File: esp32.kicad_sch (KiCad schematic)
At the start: 24 parts, among them J12 DAT0, J13 DAT_DSP, J14 + -, Q18 2N3904, Q19 2N3904, Q20 2N3904, U10 74LS241, U11 74LS241, U12 74LS241, U15 74LS241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

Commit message: smaller resistor footprint
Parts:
- R100, R90, R91, R95, R96, R97, R98, R99: footprint Resistor_THT:R_Axial_DIN0207_L6.3mm_D2.5mm_P10.16mm_Horizontal -> Resistor_THT:R_Axial_DIN0207_L6.3mm_D2.5mm_P2.54mm_Vertical
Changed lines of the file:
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@@
     (property "Reference" "R95" (id 0) (at 110.49 121.0142 90))
     (property "Value" "1k" (id 1) (at 110.49 123.5511 90))
-    (property "Footprint" "Resistor_THT:R_Axial_DIN0207_L6.3mm_D2.5mm_P10.16mm_Horizontal" (id 2) (at 110.49 127.508 90)
+    (property "Footprint" "Resistor_THT:R_Axial_DIN0207_L6.3mm_D2.5mm_P2.54mm_Vertical" (id 2) (at 110.49 127.508 90)
       (effects (font (size 1.27 1.27)) hide)
     )
@@
       (effects (font (size 1.27 1.27)) (justify left))
     )
-    (property "Footprint" "Resistor_THT:R_Axial_DIN0207_L6.3mm_D2.5mm_P10.16mm_Horizontal" (id 2) (at 122.682 114.3 90)
+    (property "Footprint" "Resistor_THT:R_Axial_DIN0207_L6.3mm_D2.5mm_P2.54mm_Vertical" (id 2) (at 122.682 114.3 90)
       (effects (font (size 1.27 1.27)) hide)
     )
@@
       (effects (font (size 1.27 1.27)) (justify left))
     )
-    (property "Footprint" "Resistor_THT:R_Axial_DIN0207_L6.3mm_D2.5mm_P10.16mm_Horizontal" (id 2) (at 99.822 63.5 90)
+    (property "Footprint" "Resistor_THT:R_Axial_DIN0207_L6.3mm_D2.5mm_P2.54mm_Vertical" (id 2) (at 99.822 63.5 90)
       (effects (font (size 1.27 1.27)) hide)
     )
@@
       (effects (font (size 1.27 1.27)) (justify left))
     )
-    (property "Footprint" "Resistor_THT:R_Axial_DIN0207_L6.3mm_D2.5mm_P10.16mm_Horizontal" (id 2) (at 134.112 168.91 90)
+    (property "Footprint" "Resistor_THT:R_Axial_DIN0207_L6.3mm_D2.5mm_P2.54mm_Vertical" (id 2) (at 134.112 168.91 90)
       (effects (font (size 1.27 1.27)) hide)
     )
@@
     (property "Reference" "R96" (id 0) (at 111.76 53.7042 90))
     (property "Value" "1k" (id 1) (at 111.76 56.2411 90))
-    (property "Footprint" "Resistor_THT:R_Axial_DIN0207_L6.3mm_D2.5mm_P10.16mm_Horizontal" (id 2) (at 111.76 60.198 90)
+    (property "Footprint" "Resistor_THT:R_Axial_DIN0207_L6.3mm_D2.5mm_P2.54mm_Vertical" (id 2) (at 111.76 60.198 90)
       (effects (font (size 1.27 1.27)) hide)
     )
@@
       (effects (font (size 1.27 1.27)) (justify left))
     )
-    (property "Footprint" "Resistor_THT:R_Axial_DIN0207_L6.3mm_D2.5mm_P10.16mm_Horizontal" (id 2) (at 98.552 130.81 90)
+    (property "Footprint" "Resistor_THT:R_Axial_DIN0207_L6.3mm_D2.5mm_P2.54mm_Vertical" (id 2) (at 98.552 130.81 90)
       (effects (font (size 1.27 1.27)) hide)
     )
@@
       (effects (font (size 1.27 1.27)) (justify left))
     )
-    (property "Footprint" "Resistor_THT:R_Axial_DIN0207_L6.3mm_D2.5mm_P10.16mm_Horizontal" (id 2) (at 123.952 46.99 90)
+    (property "Footprint" "Resistor_THT:R_Axial_DIN0207_L6.3mm_D2.5mm_P2.54mm_Vertical" (id 2) (at 123.952 46.99 90)
       (effects (font (size 1.27 1.27)) hide)
     )
@@
     (property "Reference" "R100" (id 0) (at 149.86 175.6242 90))
     (property "Value" "220k" (id 1) (at 149.86 178.1611 90))
-    (property "Footprint" "Resistor_THT:R_Axial_DIN0207_L6.3mm_D2.5mm_P10.16mm_Horizontal" (id 2) (at 149.86 182.118 90)
-      (effects (font (size 1.27 1.27)) hide)
-    )
+    (property "Footprint" "Resistor_THT:R_Axial_DIN0207_L6.3mm_D2.5mm_P2.54mm_Vertical" (id 2) (at 149.86 182.118 90)
+      (effects (font (size 1.27 1.27)) hide)
+    )

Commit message: misc updates
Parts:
- removed J13: DAT_DSP, Connector_PinHeader_2.54mm:PinHeader_1x14_P2.54mm_Vertical, symbol Connector_Generic:Conn_01x14
- added J13: DAT_DSP_1..8, Connector_PinHeader_2.54mm:PinHeader_1x08_P2.54mm_Vertical, symbol Connector_Generic:Conn_01x08
- added J15: DAT_DSP_9..14, Connector_PinHeader_2.54mm:PinHeader_1x06_P2.54mm_Vertical, symbol Connector_Generic:Conn_01x06
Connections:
- net DAT_DSP1: now also J13.1 (Pin_1)
- net DAT_DSP10: now also J15.2 (Pin_2)
- net DAT_DSP11: now also J15.3 (Pin_3)
- net DAT_DSP12: now also J15.4 (Pin_4)
- net DAT_DSP13: now also J15.5 (Pin_5)
- net DAT_DSP14: now also J15.6 (Pin_6)
- net DAT_DSP2: now also J13.2 (Pin_2)
- net DAT_DSP3: now also J13.3 (Pin_3)
- net DAT_DSP4: now also J13.4 (Pin_4)
- net DAT_DSP5: now also J13.5 (Pin_5)
- net DAT_DSP6: now also J13.6 (Pin_6)
- net DAT_DSP7: now also J13.7 (Pin_7)
- net DAT_DSP8: now also J13.8 (Pin_8)
- net DAT_DSP9: now also J15.1 (Pin_1)

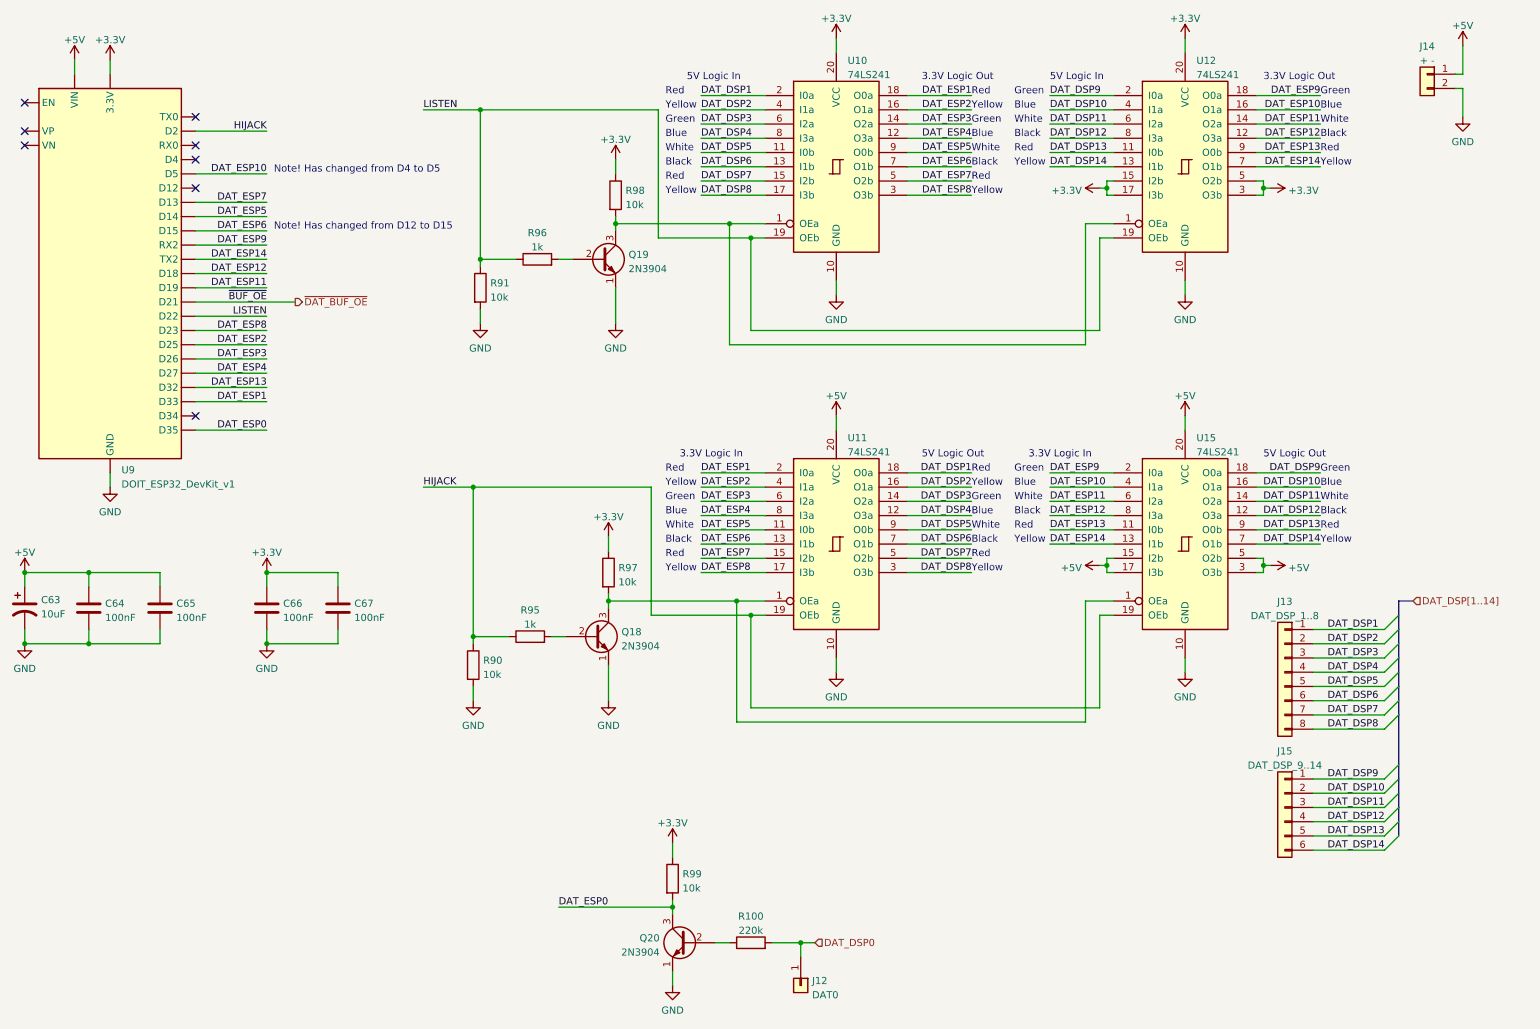
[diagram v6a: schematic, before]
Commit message: cleanup and rename subsheets, increment rev
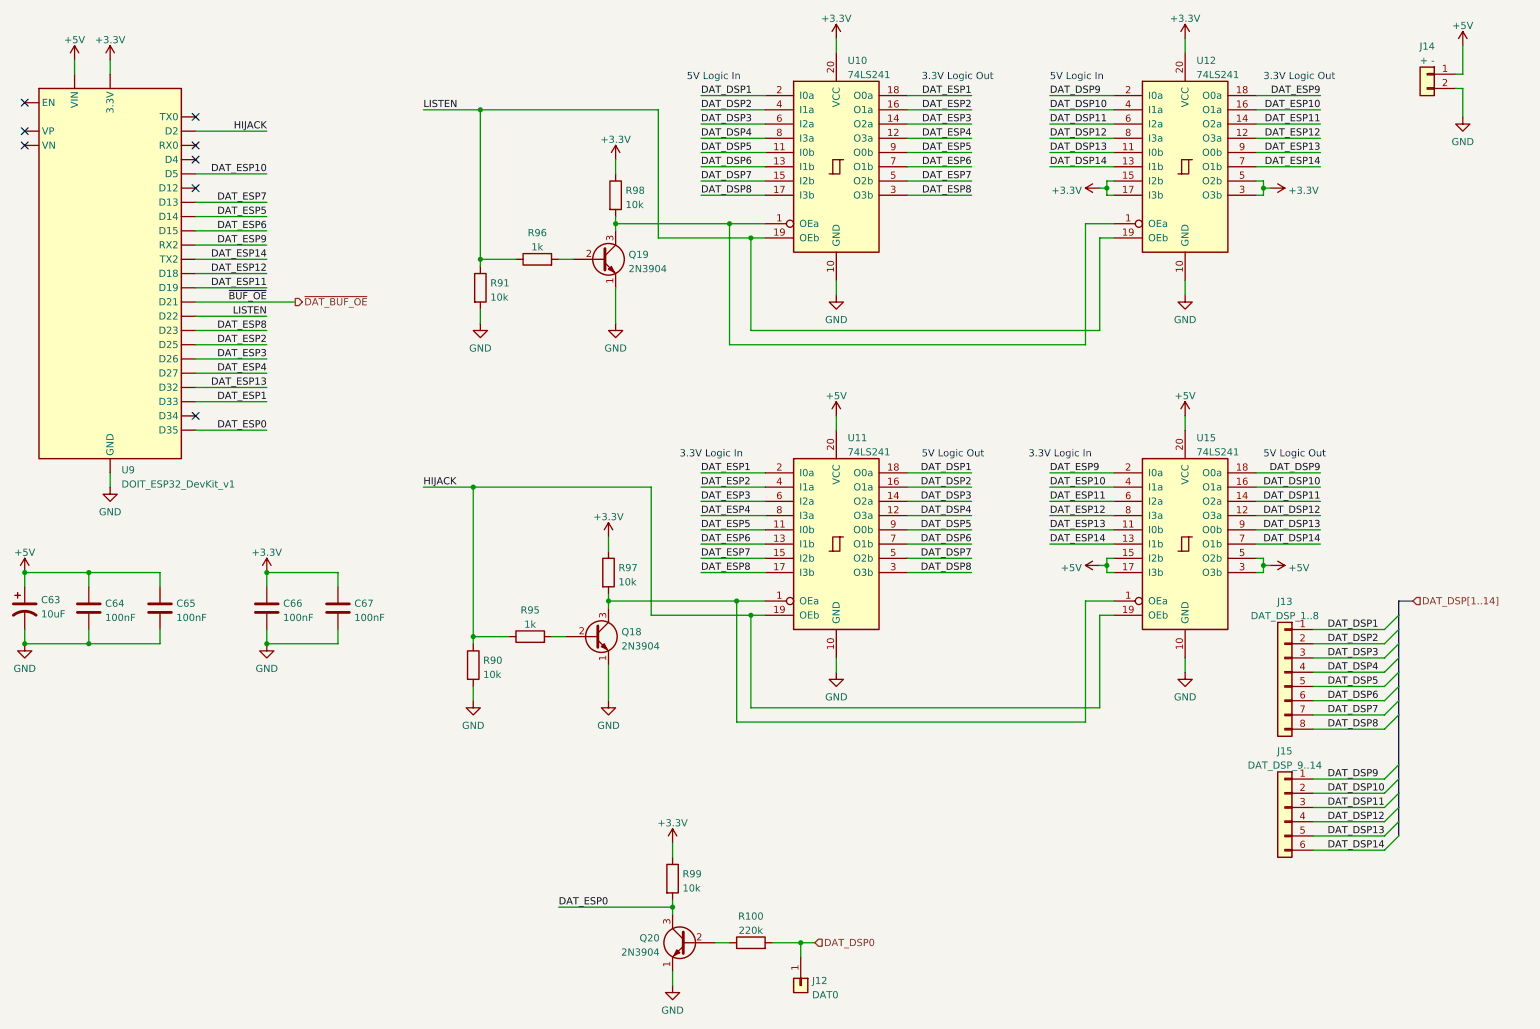
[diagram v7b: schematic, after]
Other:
- note removed: "Black"
- note removed: "Blue"
- note removed: "Green"
- note removed: "Note! Has changed from D12 to D15"
- note removed: "Note! Has changed from D4 to D5"
- note removed: "Red"
- note removed: "White"
- note removed: "Yellow"
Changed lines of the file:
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@@
 (kicad_sch (version 20211123) (generator eeschema)
   (paper "A4")
+  (title_block
+    (date "2023-07-19")
+    (rev "4")
+  )
   (junction (at 149.86 54.61) (diameter 0) (color 0 0 0 0)
   )
@@
     )
   )
-  (text "Green" (at 134.62 34.29 0)
-    (effects (font (size 1.27 1.27)) (justify left bottom))
-  )
-  (text "Green" (at 134.62 101.6 0)
-    (effects (font (size 1.27 1.27)) (justify left bottom))
-  )
-  (text "Green" (at 251.46 29.21 0)
-    (effects (font (size 1.27 1.27)) (justify left bottom))
-  )
-  (text "Red" (at 134.62 111.76 0)
-    (effects (font (size 1.27 1.27)) (justify left bottom))
-  )
-  (text "Blue" (at 196.85 31.75 0)
-    (effects (font (size 1.27 1.27)) (justify left bottom))
-  )
-  (text "Blue" (at 196.85 99.06 0)
-    (effects (font (size 1.27 1.27)) (justify left bottom))
-  )
-  (text "Red" (at 134.62 96.52 0)
-    (effects (font (size 1.27 1.27)) (justify left bottom))
-  )
-  (text "Red" (at 134.62 44.45 0)
-    (effects (font (size 1.27 1.27)) (justify left bottom))
-  )
-  (text "White" (at 134.62 106.68 0)
-    (effects (font (size 1.27 1.27)) (justify left bottom))
-  )
-  (text "Blue" (at 251.46 31.75 0)
-    (effects (font (size 1.27 1.27)) (justify left bottom))
-  )
   (text "3.3V Logic In" (at 137.16 93.98 0)
     (effects (font (size 1.27 1.27)) (justify left bottom))
   )
-  (text "White" (at 196.85 34.29 0)
-    (effects (font (size 1.27 1.27)) (justify left bottom))
-  )
   (text "3.3V Logic Out" (at 241.3 26.67 0)
     (effects (font (size 1.27 1.27)) (justify left bottom))
   )
-  (text "Yellow" (at 251.46 41.91 0)
-    (effects (font (size 1.27 1.27)) (justify left bottom))
-  )
-  (text "Black" (at 196.85 104.14 0)
-    (effects (font (size 1.27 1.27)) (justify left bottom))
-  )
-  (text "Red" (at 196.85 106.68 0)
-    (effects (font (size 1.27 1.27)) (justify left bottom))
-  )
-  (text "Note! Has changed from D12 to D15" (at 64.77 53.34 0)
-    (effects (font (size 1.27 1.27)) (justify left bottom))
-  )
-  (text "Black" (at 196.85 36.83 0)
-    (effects (font (size 1.27 1.27)) (justify left bottom))
-  )
-  (text "Green" (at 196.85 29.21 0)
-    (effects (font (size 1.27 1.27)) (justify left bottom))
-  )
-  (text "Red" (at 189.23 44.45 0)
-    (effects (font (size 1.27 1.27)) (justify left bottom))
-  )
-  (text "Blue" (at 189.23 104.14 0)
-    (effects (font (size 1.27 1.27)) (justify left bottom))
-  )
-  (text "Black" (at 189.23 109.22 0)
-    (effects (font (size 1.27 1.27)) (justify left bottom))
-  )
-  (text "White" (at 196.85 101.6 0)
-    (effects (font (size 1.27 1.27)) (justify left bottom))
-  )
-  (text "Yellow" (at 134.62 99.06 0)
-    (effects (font (size 1.27 1.27)) (justify left bottom))
-  )
-  (text "Yellow" (at 196.85 41.91 0)
-    (effects (font (size 1.27 1.27)) (justify left bottom))
-  )
-  (text "Black" (at 134.62 41.91 0)
-    (effects (font (size 1.27 1.27)) (justify left bottom))
-  )
   (text "3.3V Logic In" (at 199.39 93.98 0)
     (effects (font (size 1.27 1.27)) (justify left bottom))
   )
-  (text "White" (at 134.62 39.37 0)
-    (effects (font (size 1.27 1.27)) (justify left bottom))
-  )
-  (text "White" (at 189.23 106.68 0)
-    (effects (font (size 1.27 1.27)) (justify left bottom))
-  )
-  (text "Red" (at 251.46 106.68 0)
-    (effects (font (size 1.27 1.27)) (justify left bottom))
-  )
-  (text "Red" (at 251.46 39.37 0)
-    (effects (font (size 1.27 1.27)) (justify left bottom))
-  )
-  (text "Blue" (at 134.62 104.14 0)
-    (effects (font (size 1.27 1.27)) (justify left bottom))
-  )
-  (text "Red" (at 196.85 39.37 0)
-    (effects (font (size 1.27 1.27)) (justify left bottom))
-  )
-  (text "Red" (at 189.23 29.21 0)
-    (effects (font (size 1.27 1.27)) (justify left bottom))
-  )
-  (text "Blue" (at 251.46 99.06 0)
-    (effects (font (size 1.27 1.27)) (justify left bottom))
-  )
-  (text "White" (at 251.46 101.6 0)
-    (effects (font (size 1.27 1.27)) (justify left bottom))
-  )
-  (text "Red" (at 189.23 111.76 0)
-    (effects (font (size 1.27 1.27)) (justify left bottom))
-  )
-  (text "Black" (at 251.46 36.83 0)
-    (effects (font (size 1.27 1.27)) (justify left bottom))
-  )
-  (text "Red" (at 189.23 96.52 0)
-    (effects (font (size 1.27 1.27)) (justify left bottom))
-  )
   (text "5V Logic In" (at 138.43 26.67 0)
     (effects (font (size 1.27 1.27)) (justify left bottom))
   )
-  (text "Blue" (at 134.62 36.83 0)
-    (effects (font (size 1.27 1.27)) (justify left bottom))
-  )
-  (text "Yellow" (at 251.46 109.22 0)
-    (effects (font (size 1.27 1.27)) (justify left bottom))
-  )
-  (text "Note! Has changed from D4 to D5" (at 64.77 43.18 0)
-    (effects (font (size 1.27 1.27)) (justify left bottom))
-  )
-  (text "Green" (at 189.23 101.6 0)
-    (effects (font (size 1.27 1.27)) (justify left bottom))
-  )
-  (text "Green" (at 196.85 96.52 0)
-    (effects (font (size 1.27 1.27)) (justify left bottom))
-  )
-  (text "Yellow" (at 189.23 46.99 0)
-    (effects (font (size 1.27 1.27)) (justify left bottom))
-  )
   (text "3.3V Logic Out" (at 180.34 26.67 0)
     (effects (font (size 1.27 1.27)) (justify left bottom))
   )
-  (text "Yellow" (at 189.23 114.3 0)
-    (effects (font (size 1.27 1.27)) (justify left bottom))
-  )
-  (text "Green" (at 189.23 34.29 0)
-    (effects (font (size 1.27 1.27)) (justify left bottom))
-  )
-  (text "Green" (at 251.46 96.52 0)
-    (effects (font (size 1.27 1.27)) (justify left bottom))
-  )
-  (text "Blue" (at 189.23 36.83 0)
-    (effects (font (size 1.27 1.27)) (justify left bottom))
-  )
   (text "5V Logic In" (at 203.2 26.67 0)
     (effects (font (size 1.27 1.27)) (justify left bottom))
   )
-  (text "Yellow" (at 134.62 31.75 0)
-    (effects (font (size 1.27 1.27)) (justify left bottom))
-  )
-  (text "Yellow" (at 134.62 46.99 0)
-    (effects (font (size 1.27 1.27)) (justify left bottom))
-  )
-  (text "White" (at 189.23 39.37 0)
-    (effects (font (size 1.27 1.27)) (justify left bottom))
-  )
-  (text "Black" (at 134.62 109.22 0)
-    (effects (font (size 1.27 1.27)) (justify left bottom))
-  )
-  (text "Yellow" (at 134.62 114.3 0)
-    (effects (font (size 1.27 1.27)) (justify left bottom))
-  )
-  (text "White" (at 251.46 34.29 0)
-    (effects (font (size 1.27 1.27)) (justify left bottom))
-  )
-  (text "Yellow" (at 189.23 31.75 0)
-    (effects (font (size 1.27 1.27)) (justify left bottom))
-  )
-  (text "Black" (at 251.46 104.14 0)
-    (effects (font (size 1.27 1.27)) (justify left bottom))
-  )
-  (text "Red" (at 134.62 29.21 0)
-    (effects (font (size 1.27 1.27)) (justify left bottom))
-  )
-  (text "Yellow" (at 196.85 109.22 0)
-    (effects (font (size 1.27 1.27)) (justify left bottom))
-  )
-  (text "Black" (at 189.23 41.91 0)
-    (effects (font (size 1.27 1.27)) (justify left bottom))
-  )
   (text "5V Logic Out" (at 241.3 93.98 0)
     (effects (font (size 1.27 1.27)) (justify left bottom))
   )
-  (text "Yellow" (at 189.23 99.06 0)
-    (effects (font (size 1.27 1.27)) (justify left bottom))
-  )
